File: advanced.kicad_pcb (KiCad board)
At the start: 2 copper layers, 108 parts, among them U1 ATtiny24-20P, U2 ATtiny28L-4P, U3 ATtiny13A-P, U4 ATtiny25-20P, U5 ATtiny24-20P, U6 ATtiny85-20P

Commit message: minor imporvements
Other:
- board text added: "CABLE"
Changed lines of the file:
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@@
     )
   )
-  (gr_line (start 240.284 89.916) (end 240.284 123.952) (layer "F.SilkS") (width 0.15))
+  (gr_line (start 248.92 91.948) (end 247.904 91.44) (layer "B.SilkS") (width 0.12))
+  (gr_line (start 248.92 91.948) (end 247.904 92.456) (layer "B.SilkS") (width 0.12))
+  (gr_line (start 244.856 91.948) (end 248.412 91.948) (layer "B.SilkS") (width 0.12))
+  (gr_line (start 240.284 88.9) (end 240.284 123.952) (layer "F.SilkS") (width 0.15))
   (gr_line (start 196.088 73.152) (end 221.488 81.788) (layer "F.SilkS") (width 0.15))
   (gr_line (start 125.73 142.875) (end 104.14 127.635) (layer "F.SilkS") (width 0.15))
@@
   (gr_line (start 176.276 120.396) (end 141.224 56.388) (layer "F.SilkS") (width 0.15))
   (gr_line locked (start 125.984 129.032) (end 124.46 120.396) (layer "F.SilkS") (width 0.15))
-  (gr_line (start 240.284 89.916) (end 265.684 89.916) (layer "F.SilkS") (width 0.15))
+  (gr_line (start 240.284 88.9) (end 265.684 88.9) (layer "F.SilkS") (width 0.15))
   (gr_line (start 111.125 81.915) (end 103.124 84.328) (layer "F.SilkS") (width 0.15))
   (gr_line (start 120.015 120.65) (end 120.65 128.905) (layer "F.SilkS") (width 0.15))
@@
   (gr_line (start 100.33 155.575) (end 102.235 145.415) (layer "F.SilkS") (width 0.15))
   (gr_line (start 192.024 154.432) (end 135.636 142.748) (layer "F.SilkS") (width 0.15))
+  (gr_text "CABLE" (at 246.888 89.916) (layer "B.SilkS")
+    (effects (font (size 1 1) (thickness 0.15)) (justify mirror))
+  )
   (gr_text "by phuid & Milda" (at 198.12 148.336) (layer "F.SilkS")
     (effects (font (size 2 2) (thickness 0.15)))
@@
   (segment (start 211.455 124.46) (end 214.63 121.285) (width 0.2) (layer "B.Cu") (net 0))
   (segment (start 258.064 106.68) (end 258.064 120.396) (width 0.2) (layer "B.Cu") (net 0))
+  (segment (start 151.13 128.905) (end 169.545 147.32) (width 0.2) (layer "B.Cu") (net 0))
   (segment (start 238.76 116.84) (end 238.76 108.585) (width 0.2) (layer "B.Cu") (net 0))
-  (segment (start 254.508 145.796) (end 252.984 147.32) (width 0.2) (layer "B.Cu") (net 0))
   (segment (start 186.055001 56.514999) (end 188.595 53.975) (width 0.2) (layer "B.Cu") (net 0))
   (segment (start 188.595 53.975) (end 235.585 53.975) (width 0.2) (layer "B.Cu") (net 0))
   (segment (start 253.238 149.098) (end 172.466 149.098) (width 0.2) (layer "B.Cu") (net 0))
   (segment (start 247.65 105.41) (end 248.28 104.78) (width 0.2) (layer "B.Cu") (net 0))
-  (segment (start 255.4605 106.2355) (end 255.4605 106.6165) (width 0.2) (layer "B.Cu") (net 0))
   (segment (start 243.84 94.615) (end 244.475 95.25) (width 0.2) (layer "B.Cu") (net 0))
   (segment (start 172.466 149.098) (end 169.164 152.4) (width 0.2) (layer "B.Cu") (net 0))
+  (segment (start 252.984 147.32) (end 254.508 145.796) (width 0.2) (layer "B.Cu") (net 0))
+  (segment (start 169.545 147.32) (end 252.984 147.32) (width 0.2) (layer "B.Cu") (net 0))
   (segment (start 125.73 71.12) (end 125.73 56.515) (width 0.2) (layer "B.Cu") (net 0))
+  (segment (start 256.54 107.315) (end 248.28 99.055) (width 0.2) (layer "B.Cu") (net 0))
   (segment (start 221.488 110.2245) (end 221.488 94.2455) (width 0.2) (layer "B.Cu") (net 0))
   (segment (start 221.488 94.2455) (end 218.6825 91.44) (width 0.2) (layer "B.Cu") (net 0))
@@
   (segment (start 248.28 101.595) (end 246.888 100.203) (width 0.2) (layer "B.Cu") (net 0))
   (segment (start 246.888 100.203) (end 246.888 98.044) (width 0.2) (layer "B.Cu") (net 0))
-  (segment (start 254.508 121.92) (end 254.508 145.796) (width 0.2) (layer "B.Cu") (net 0))
   (segment (start 247.015 95.25) (end 248.28 96.515) (width 0.2) (layer "B.Cu") (net 0))
   (segment (start 248.28 104.78) (end 248.28 104.135) (width 0.2) (layer "B.Cu") (net 0))
@@
   (segment (start 218.6825 113.03) (end 221.488 110.2245) (width 0.2) (layer "B.Cu") (net 0))
   (segment (start 255.905 69.215) (end 255.905 86.35) (width 0.2) (layer "B.Cu") (net 0))
-  (segment (start 169.545 147.32) (end 151.13 128.905) (width 0.2) (layer "B.Cu") (net 0))
   (segment (start 246.888 98.044) (end 247.396 97.536) (width 0.2) (layer "B.Cu") (net 0))
-  (segment (start 256.54 107.696) (end 256.54 119.888) (width 0.2) (layer "B.Cu") (net 0))
   (segment (start 186.055001 73.024999) (end 186.055001 56.514999) (width 0.2) (layer "B.Cu") (net 0))
-  (segment (start 248.28 99.055) (end 255.4605 106.2355) (width 0.2) (layer "B.Cu") (net 0))
   (segment (start 255.905 86.35) (end 248.28 93.975) (width 0.2) (layer "B.Cu") (net 0))
-  (segment (start 256.54 119.888) (end 254.508 121.92) (width 0.2) (layer "B.Cu") (net 0))
   (segment (start 241.935 105.41) (end 247.65 105.41) (width 0.2) (layer "B.Cu") (net 0))
+  (segment (start 254.508 145.796) (end 254.508 121.92) (width 0.2) (layer "B.Cu") (net 0))
   (segment (start 132.08 50.165) (end 236.855 50.165) (width 0.2) (layer "B.Cu") (net 0))
   (segment (start 169.164 152.4) (end 103.505 152.4) (width 0.2) (layer "B.Cu") (net 0))
@@
   (segment (start 236.855 50.165) (end 255.905 69.215) (width 0.2) (layer "B.Cu") (net 0))
   (segment (start 234.315 121.285) (end 238.76 116.84) (width 0.2) (layer "B.Cu") (net 0))
-  (segment (start 255.4605 106.6165) (end 256.54 107.696) (width 0.2) (layer "B.Cu") (net 0))
+  (segment (start 256.54 119.888) (end 256.54 107.315) (width 0.2) (layer "B.Cu") (net 0))
   (segment (start 255.524 122.936) (end 255.524 146.812) (width 0.2) (layer "B.Cu") (net 0))
-  (segment (start 252.984 147.32) (end 169.545 147.32) (width 0.2) (layer "B.Cu") (net 0))
+  (segment (start 254.508 121.92) (end 256.54 119.888) (width 0.2) (layer "B.Cu") (net 0))
   (segment (start 249.936 75.311) (end 249.936 79.756) (width 0.2) (layer "F.Cu") (net 19))
   (segment (start 247.015 72.39) (end 249.936 75.311) (width 0.2) (layer "F.Cu") (net 19))

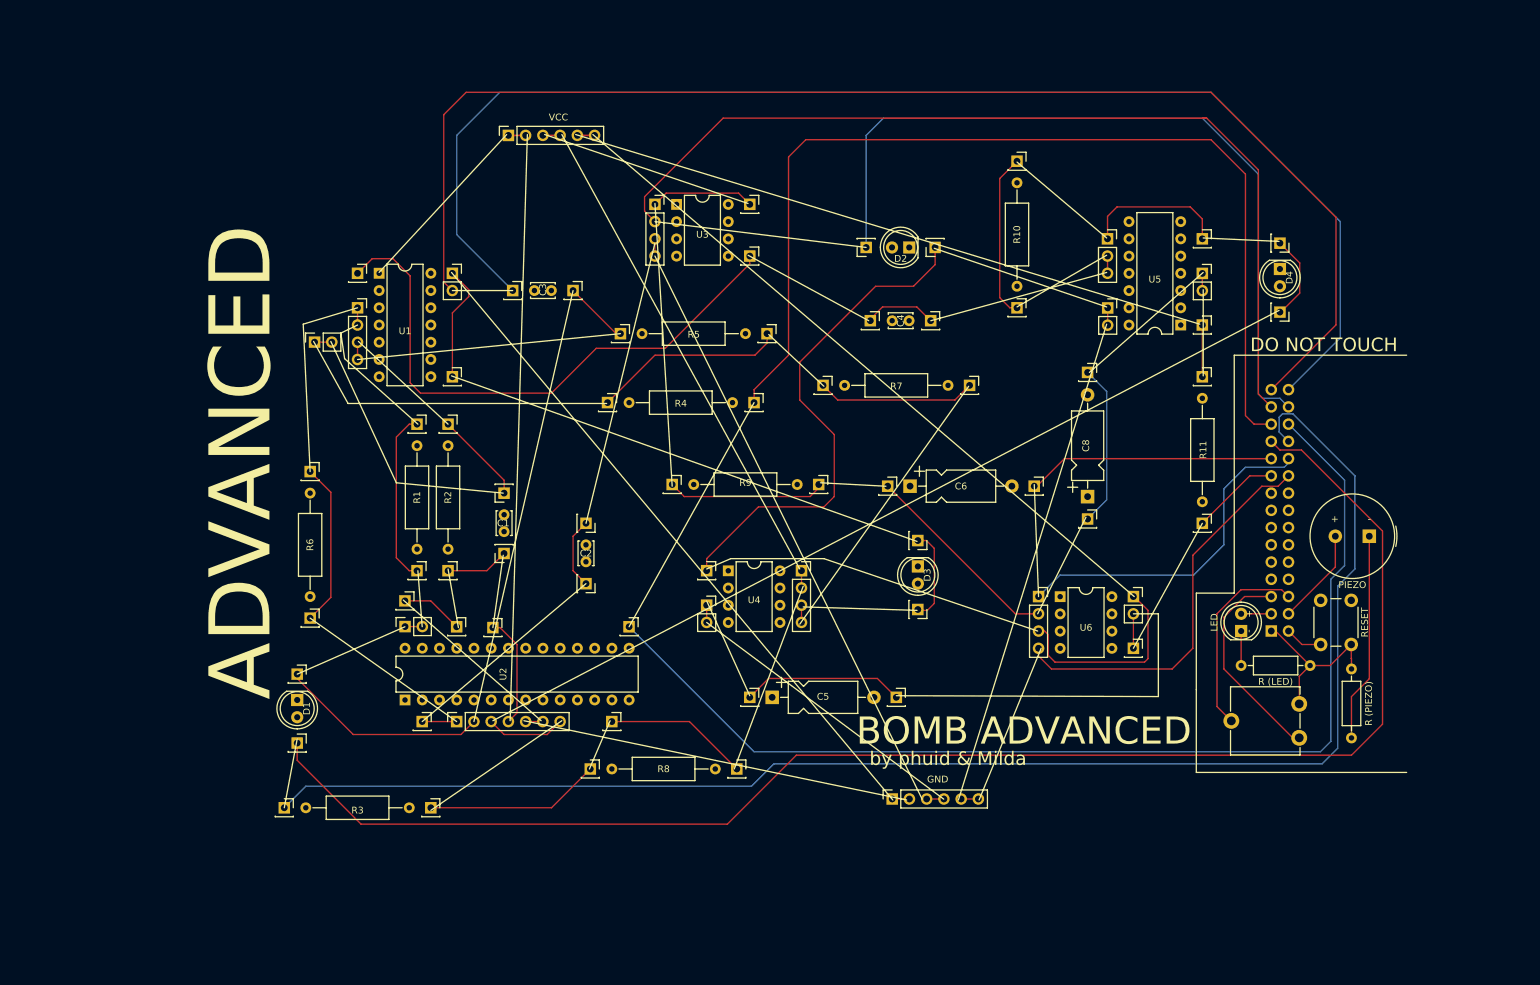
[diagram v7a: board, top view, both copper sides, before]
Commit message: single ground, part list propably doneish
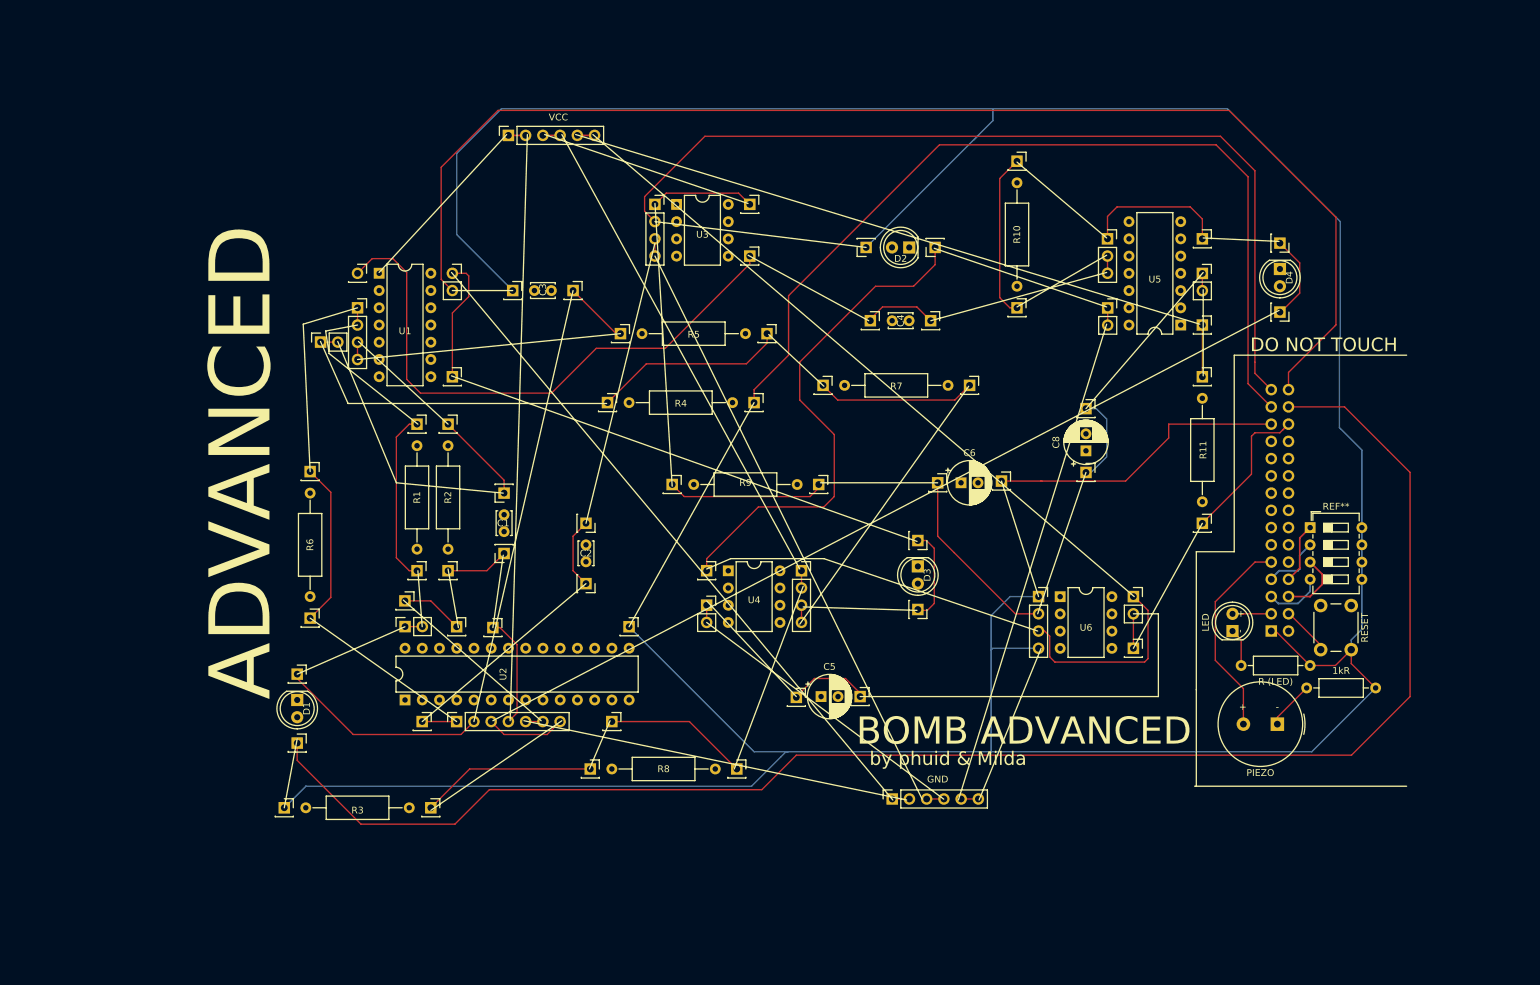
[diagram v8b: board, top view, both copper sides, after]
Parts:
- removed the REF** at (249.9, 140.3)
- added REF**: SW_DIP_SPSTx04_Slide_6.7x11.72mm_W7.62mm_P2.54mm_LowProfile, Button_Switch_THT:SW_DIP_SPSTx04_Slide_6.7x11.72mm_W7.62mm_P2.54mm_LowProfile, F.Cu at (251.5, 114.3)
- 1kR: renamed from R (PIEZO)
- C5, C6, C8: footprint Capacitor_THT:CP_Axial_L10.0mm_D4.5mm_P15.00mm_Horizontal -> Capacitor_THT:CP_Radial_D6.3mm_P2.50mm
- R10: value R -> 2000
- moved PIEZO 30.8 mm to (246.6, 143.3)
- moved 1kR 8.18 mm to (261.1, 137.9), turned to 180 degrees
- moved C6 7.53 mm to (200.0, 107.7)
- moved   7.38 mm to (196.6, 107.7)
- moved C5 7.21 mm to (179.4, 139.2)
- moved   6.86 mm to (218.4, 106.2)
- moved   6.86 mm to (175.8, 139.3)
- moved C8 6.75 mm to (218.4, 103.0)
- moved   5.34 mm to (218.4, 96.8)
- moved   5.34 mm to (185.2, 139.2)
- moved   4.88 mm to (206.0, 107.4)
- moved LED 1.27 mm to (240.0, 129.5)
- moved REF** 0.89 mm to (105.7, 87.0)
- moved RESET 0.76 mm to (257.5, 125.8)
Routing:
- net (no net): track 2426.6 -> 2063.7 mm
